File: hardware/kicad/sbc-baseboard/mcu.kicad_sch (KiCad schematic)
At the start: 36 parts, among them J16 SWD, J3 USB-C HID to target, SW201 RESET, U201 MK64FN1M0VLL12, U202 USBLC6-2SC6, Y201 32.768kHz

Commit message: Re-lay out every sheet around its main component
Nets fan out of each hub IC as wires at pin pitch; connectors, series
parts, pull-ups and power symbols sit at the lane ends, and labels are
kept for nets that leave the page. Supply pins share a bus with their
decoupling; ESD arrays sit on the connector's D-/D+ rows and port
switches on the VBUS row, so every wire into a receptacle is straight;
the stacked USB-A is a two-unit symbol, one per port. Relays move to
their own sheet (8xx). ESD diodes use KiCad's PESD5V0S1UL in SOD-882.

Generator: gen/fanout.py (lane engine), gen/check_geom.py (endpoint
contacts), gen/netcheck.py (wire-level rail merges). ERC, both checks
and a renumbering-tolerant netlist diff against the first pass all
clean; 331 parts, 354 nets.

Co-Authored-By: Claude Fable 5.1 <noreply@anthropic.com>
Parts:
- C201, C202: value 100n -> 2u2
- C203, C204: value 100n -> 12p
- C205: value 100n -> 1u
- C207, C208: value 10u -> 100n; footprint Capacitor_SMD:C_0805_2012Metric -> Capacitor_SMD:C_0603_1608Metric
- C210, C211: value 2u2 -> 100n
- C212: value 12p -> 10u; footprint Capacitor_SMD:C_0603_1608Metric -> Capacitor_SMD:C_0805_2012Metric
- C213: value 12p -> 100n
- C214: value 1u -> 10u; footprint Capacitor_SMD:C_0603_1608Metric -> Capacitor_SMD:C_0805_2012Metric
- R203, R204: value 5.1k -> 330
- R205: value 100k -> 330
- R206: value 47k -> 4.7k
- R207, R208, R209: value 330 -> 4.7k
- R210: value 4.7k -> 100k
- R211: value 4.7k -> 47k
- R212, R213: value 4.7k -> 5.1k
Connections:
- net +3V3: now also C206.2, C207.2, C208.2, C209.2, C210.2, C211.2, C212.2, FB201.2, R202.2, R206.1, R207.1, R208.1, R209.1; no longer C201.1, C202.1, C203.1, C204.1, C205.1, C206.1, C207.1, FB201.1, R202.1, R210.1, R211.1, R212.1, R213.1
- net +3V3A: now also C213.2, C214.2, FB201.1; no longer C208.1, C209.1, FB201.2
- net GND: now also C206.1, C207.1, C208.1, C209.1, C210.1, C211.1, C212.1, C213.1, C214.1, R211.2, R212.2, R213.2; no longer C206.2, C207.2, C208.2, C209.2, C210.2, C211.2, C212.2, C213.2, C214.2, R203.2, R204.2, R206.2
- net I2C0_SCL: now also R208.2; no longer R210.2
- net I2C0_SDA: now also R209.2; no longer R211.2
- net I2C1_SCL: now also R206.2; no longer R212.2
- net I2C1_SDA: now also R207.2; no longer R213.2
- net J3_VBUS: now also R210.1; no longer R205.1
- net K64_RESET_N: now also C205.1; no longer C214.1
- net VBUS_SENSE: now also R210.2, R211.1; no longer R205.2, R206.1
- net HB_B: no longer names the net of U201.67 (PTB21)
- net HB_B: now also R205.1; no longer R209.2
- net HB_B_K: no longer names the net of D202.3 (BK)
- net HB_B_K: now also R205.2; no longer R209.1
- net HB_G: no longer names the net of U201.66 (PTB20)
- net HB_G: now also R204.1; no longer R208.2
- net HB_G_K: no longer names the net of D202.2 (GK)
- net HB_G_K: now also R204.2; no longer R208.1
- net HB_R: no longer names the net of U201.65 (PTB19)
- net HB_R: now also R203.1; no longer R207.2
- net HB_R_K: no longer names the net of D202.1 (RK)
- net HB_R_K: now also R203.2; no longer R207.1
- net J3_CC1: no longer names the net of J3.A5 (CC1)
- net J3_CC1: now also R212.1; no longer R203.1
- net J3_CC2: no longer names the net of J3.B5 (CC2)
- net J3_CC2: now also R213.1; no longer R204.1
- net J3_DM: no longer names the net of J3.A7 (D-), J3.B7 (D-)
- net J3_DM: now also U202.1 (I/O1); no longer U202.3 (I/O2)
- net J3_DP: no longer names the net of J3.A6 (D+), J3.B6 (D+)
- net J3_DP: now also U202.3 (I/O2); no longer U202.1 (I/O1)
- removed net K64_EXTAL32: C212.1, U201.29 (EXTAL32), Y201.1
- net K64_NMI_N: no longer names the net of U201.38 (NMI_b/PTA4)
- net K64_NMI_N: now also R202.1; no longer R202.2
- net K64_USB_DM: no longer names the net of U202.4 (I/O2)
- net K64_USB_DM: now also U201.10 (USB0_DP); no longer U201.11 (USB0_DM)
- net K64_USB_DP: no longer names the net of U202.6 (I/O1)
- net K64_USB_DP: now also U201.11 (USB0_DM); no longer U201.10 (USB0_DP)
- net K64_VOUT33: no longer names the net of U201.12 (VOUT33)
- net K64_VOUT33: now also C202.1; no longer C211.1
- net K64_VREGIN: no longer names the net of D201.1 (K), U201.13 (VREGIN)
- net K64_VREGIN: now also C201.1; no longer C210.1
- removed net K64_XTAL32: C213.1, U201.28 (XTAL32), Y201.2
- new net: C204.1, U201.28 (XTAL32), Y201.1
- new net: C203.1, U201.29 (EXTAL32), Y201.2

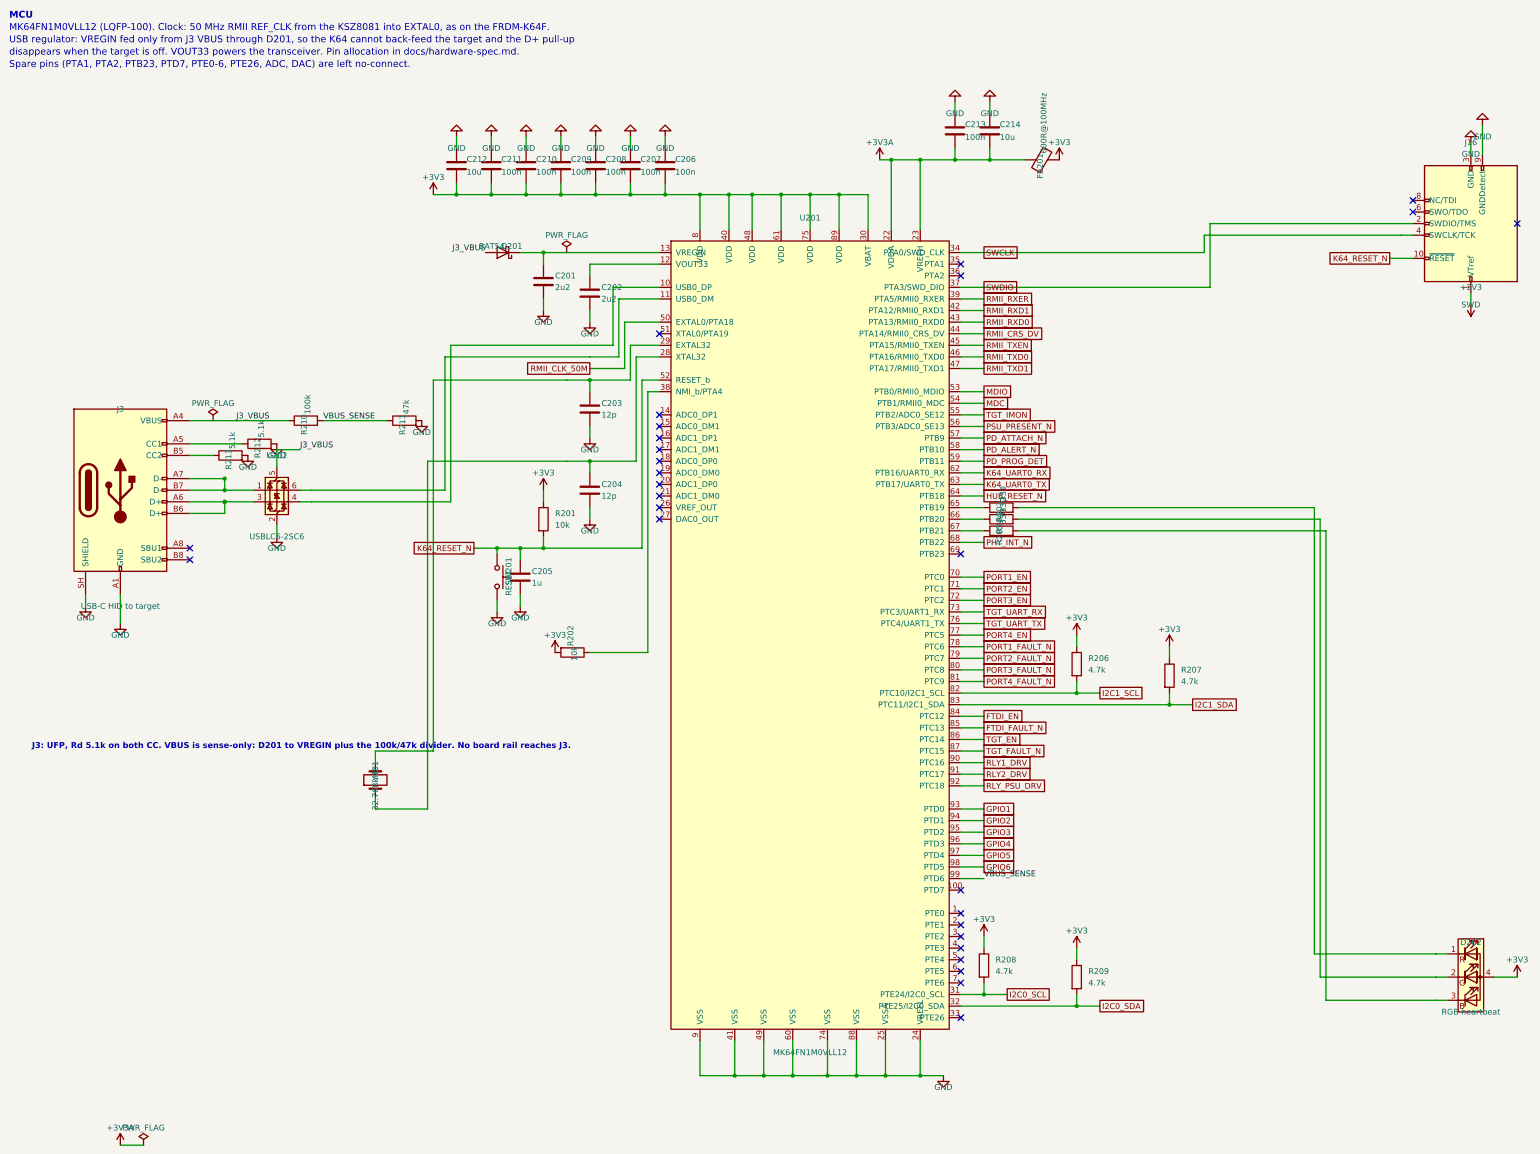
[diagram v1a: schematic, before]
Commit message: Symbol direction, field text and decoupling ladders across every sheet
Every GND symbol now hangs down and every rail stands up: decoupling
hangs from the supply bus into a GND rail with one GND symbol at the end
(ladders), rails on crowded supply pins are jogged sideways, the SWD
header is mirrored instead of rotated. Field text on in-line parts reads
horizontally (KiCad adds the symbol rotation to the field angle) and is
placed by lane direction; hanging parts carry their text on the side away
from the pin; IC reference and value sit where the library put them.
Power sheet: bus buffer moved under the STUSB4500's I2C lanes with direct
routes, programmer by label, buck drawn as a box with its input and
output capacitors as ladders. New gen/check_layout.py reports text and
wire overlaps and wrong-way power symbols; PDF export draws hop-overs.

ERC 0, no merged rails, netlist equivalent; text-overlap residue listed
in the layout checker output remains on the hub, relays and DAPLink.

Co-Authored-By: Claude Fable 5.1 <noreply@anthropic.com>
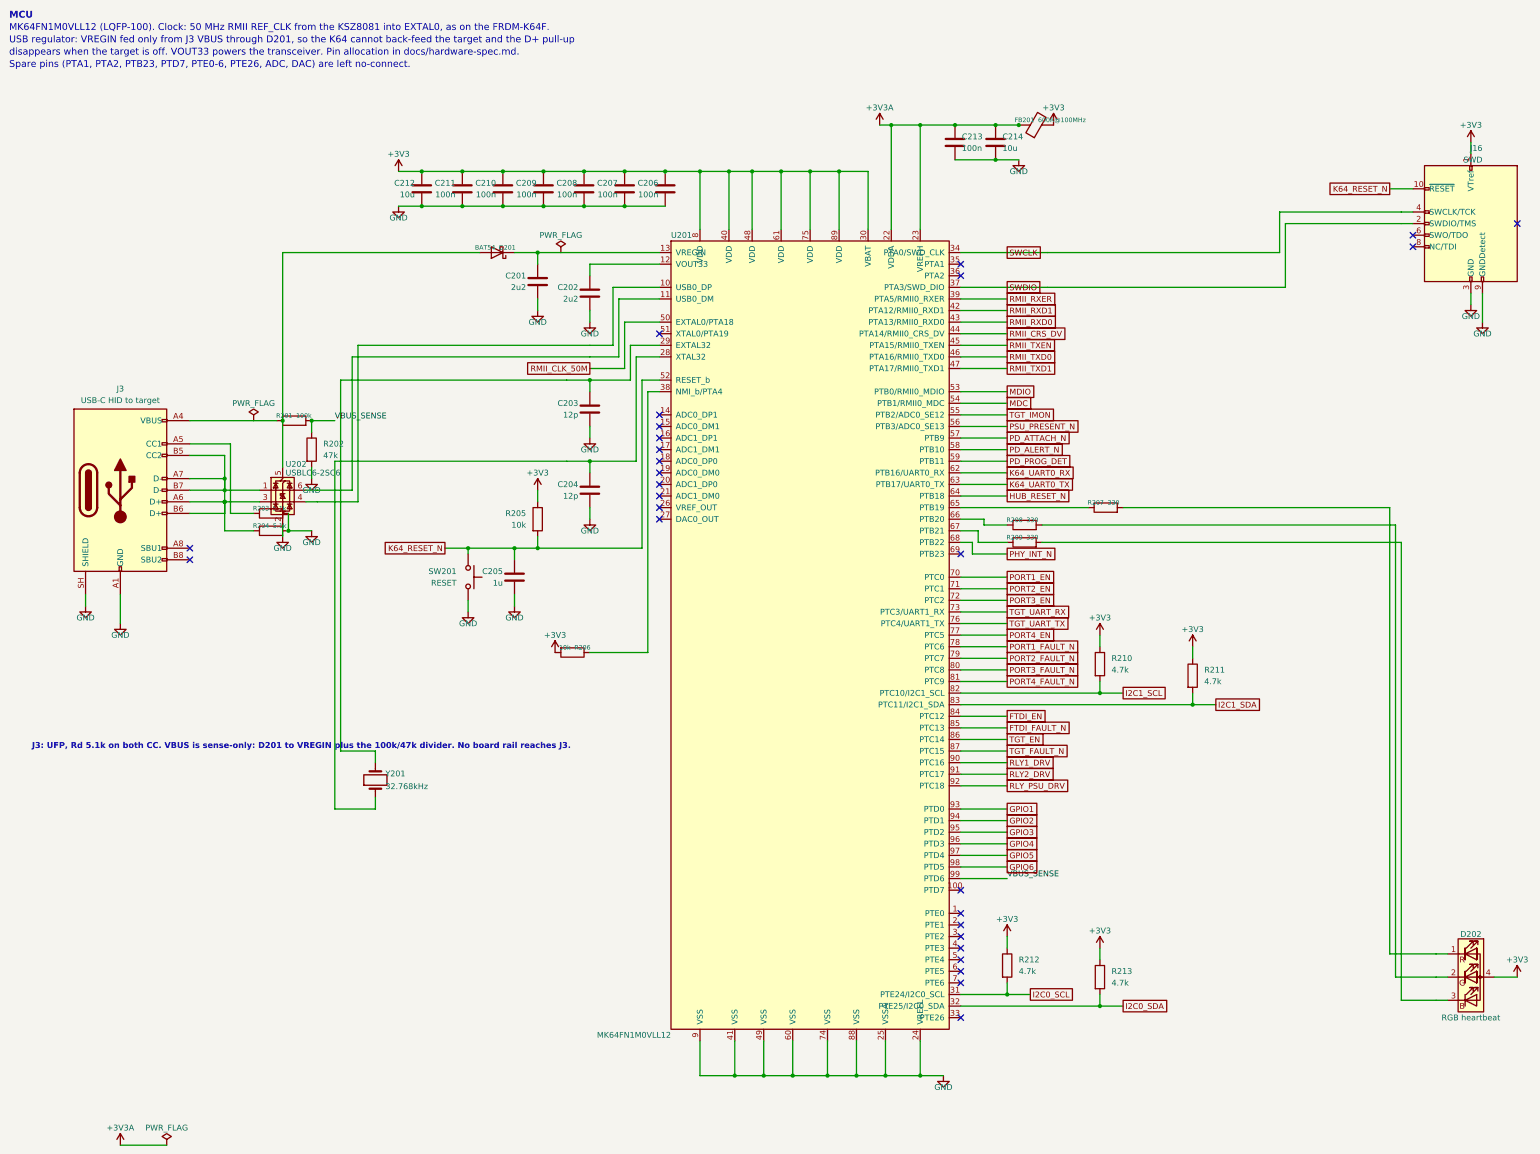
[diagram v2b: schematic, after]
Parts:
- R201: value 10k -> 100k
- R202: value 10k -> 47k
- R203, R204: value 330 -> 5.1k
- R205: value 330 -> 10k
- R206: value 4.7k -> 10k
- R207, R208, R209: value 4.7k -> 330
- R210: value 100k -> 4.7k
- R211: value 47k -> 4.7k
- R212, R213: value 5.1k -> 4.7k
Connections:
- net +3V3: now also C206.1, C207.1, C208.1, C209.1, C210.1, C211.1, C212.1, R205.1, R206.2, R210.1, R211.1, R212.1, R213.1; no longer C206.2, C207.2, C208.2, C209.2, C210.2, C211.2, C212.2, R201.1, R202.2, R206.1, R207.1, R208.1, R209.1
- net +3V3A: now also C213.1, C214.1; no longer C213.2, C214.2
- net GND: now also C206.2, C207.2, C208.2, C209.2, C210.2, C211.2, C212.2, C213.2, C214.2, R202.2, R203.2, R204.2; no longer C206.1, C207.1, C208.1, C209.1, C210.1, C211.1, C212.1, C213.1, C214.1, R211.2, R212.2, R213.2
- net I2C0_SCL: now also R212.2; no longer R208.2
- net I2C0_SDA: now also R213.2; no longer R209.2
- net I2C1_SCL: now also R210.2; no longer R206.2
- net I2C1_SDA: now also R211.2; no longer R207.2
- net K64_RESET_N: now also R205.2; no longer R201.2
- net VBUS_SENSE: now also R201.2, R202.1; no longer R210.2, R211.1
- net at D202.1 (RK): now also R207.2; no longer R203.2
- net at D202.2 (GK): now also R208.2; no longer R204.2
- net at D202.3 (BK): now also R209.2; no longer R205.2
- net at J3.A5 (CC1): now also R203.1; no longer R212.1
- net at J3.A6 (D+), J3.B6 (D+), U202.3 (I/O2): now also J3.A7 (D-), J3.B5 (CC2), J3.B7 (D-), R204.1, U202.1 (I/O1)
- net at U201.38 (NMI_b/PTA4): now also R206.1; no longer R202.1
- net at U201.67 (PTB21): now also R209.1; no longer R205.1
- net at U201.65 (PTB19): now also R207.1; no longer R203.1
- net at U201.66 (PTB20): now also R208.1; no longer R204.1
- net J3_VBUS: no longer names the net of J3.A4 (VBUS), J3.A9 (VBUS), J3.B4 (VBUS), J3.B9 (VBUS)
- net J3_VBUS: now also R201.1; no longer D201.2 (A), R210.1, U202.5 (VBUS)
- new net: D201.2 (A), U202.5 (VBUS)
